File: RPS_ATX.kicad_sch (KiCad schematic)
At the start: 32 parts, among them J1 5V, J2 C1, J3 C2, J4 17.5V, J5 PS_OUT-, J6 PS_OUT+, J7 RPS_OUT+, J9 RPS_OUT-, Q1 AO3400A, U2 AMS1117-3.3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

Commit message: approximate location of the components at the PCB
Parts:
- removed C17: 100n, Capacitor_SMD:C_0805_2012Metric_Pad1.18x1.45mm_HandSolder, symbol Device:C
- added R20: 5.1K, Resistor_SMD:R_1206_3216Metric_Pad1.30x1.75mm_HandSolder, symbol Device:R
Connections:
- net MCU_DCH: now also R20.2
- net MEAS_I+: now also R20.1
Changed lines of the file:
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@@
 	)
 	(junction
+		(at 111.76 63.5)
+		(diameter 0)
+		(color 0 0 0 0)
+	)
+	(junction
 		(at 208.28 30.48)
 		(diameter 0)
@@
 	)
 	(junction
+		(at 111.76 55.88)
+		(diameter 0)
+		(color 0 0 0 0)
+	)
+	(junction
 		(at 63.5 87.63)
 		(diameter 0)
@@
 	)
 	(junction
-		(at 24.13 87.63)
-		(diameter 0)
-		(color 0 0 0 0)
-	)
-	(junction
 		(at 158.75 88.9)
 		(diameter 0)
@@
 	)
 	(junction
-		(at 31.75 87.63)
-		(diameter 0)
-		(color 0 0 0 0)
-	)
-	(junction
 		(at 73.66 149.86)
 		(diameter 0)
@@
 	)
 	(junction
-		(at 31.75 96.52)
+		(at 63.5 149.86)
 		(diameter 0)
 		(color 0 0 0 0)
 	)
 	(junction
-		(at 63.5 149.86)
+		(at 24.13 87.63)
 		(diameter 0)
 		(color 0 0 0 0)
@@
 	(wire
 		(pts
-			(xy 48.26 39.37) (xy 128.27 39.37)
+			(xy 24.13 87.63) (xy 24.13 88.9)
 		)
 		(stroke
@@
 	(wire
 		(pts
-			(xy 196.85 30.48) (xy 208.28 30.48)
+			(xy 48.26 39.37) (xy 128.27 39.37)
 		)
 		(stroke
@@
 	(wire
 		(pts
-			(xy 24.13 87.63) (xy 31.75 87.63)
+			(xy 196.85 30.48) (xy 208.28 30.48)
 		)
 		(stroke
@@
 	(wire
 		(pts
-			(xy 31.75 96.52) (xy 48.26 96.52)
-		)
-		(stroke
-			(width 0)
-			(type default)
-		)
-	)
-	(wire
-		(pts
 			(xy 48.26 127) (xy 48.26 129.54)
 		)
@@
 	(wire
 		(pts
-			(xy 31.75 87.63) (xy 31.75 88.9)
+			(xy 48.26 96.52) (xy 63.5 96.52)
 		)
 		(stroke
@@
 	(wire
 		(pts
-			(xy 48.26 96.52) (xy 63.5 96.52)
+			(xy 48.26 49.53) (xy 48.26 48.26)
 		)
 		(stroke
@@
 	(wire
 		(pts
-			(xy 48.26 49.53) (xy 48.26 48.26)
+			(xy 35.56 49.53) (xy 38.1 49.53)
 		)
 		(stroke
@@
 	(wire
 		(pts
-			(xy 35.56 49.53) (xy 38.1 49.53)
+			(xy 48.26 158.75) (xy 48.26 161.29)
 		)
 		(stroke
@@
 	(wire
 		(pts
-			(xy 48.26 158.75) (xy 48.26 161.29)
+			(xy 142.24 63.5) (xy 142.24 49.53)
 		)
 		(stroke
@@
 	(wire
 		(pts
-			(xy 142.24 63.5) (xy 142.24 49.53)
+			(xy 142.24 49.53) (xy 147.32 49.53)
 		)
 		(stroke
@@
 	(wire
 		(pts
-			(xy 142.24 49.53) (xy 147.32 49.53)
+			(xy 74.93 59.69) (xy 73.66 59.69)
 		)
 		(stroke
@@
 	(wire
 		(pts
-			(xy 74.93 59.69) (xy 73.66 59.69)
+			(xy 40.64 87.63) (xy 24.13 87.63)
 		)
 		(stroke
@@
 	(wire
 		(pts
-			(xy 31.75 87.63) (xy 40.64 87.63)
+			(xy 111.76 63.5) (xy 128.27 63.5)
 		)
 		(stroke
@@
 	(wire
 		(pts
-			(xy 24.13 87.63) (xy 24.13 88.9)
-		)
-		(stroke
-			(width 0)
-			(type default)
-		)
-	)
-	(wire
-		(pts
 			(xy 137.16 104.14) (xy 133.35 104.14)
 		)
@@
 	(wire
 		(pts
-			(xy 95.25 63.5) (xy 128.27 63.5)
+			(xy 95.25 63.5) (xy 111.76 63.5)
 		)
 		(stroke
@@
 	(wire
 		(pts
-			(xy 24.13 96.52) (xy 31.75 96.52)
+			(xy 24.13 96.52) (xy 48.26 96.52)
 		)
 		(stroke
@@
 	)
 	(symbol
+		(lib_id "Device:R")
+		(at 111.76 59.69 180)
+		(unit 1)
+		(exclude_from_sim no)
+		(in_bom yes)
+		(on_board yes)
+		(dnp no)
+		(property "Reference" "R20"
+			(at 107.442 65.024 0)
+			(effects
+				(font
+					(size 1.27 1.27)
+				)
+				(justify right)
+			)
+		)
+		(property "Value" "5.1K"
+			(at 107.442 67.564 0)
+			(effects
+				(font
+					(size 1.27 1.27)
+				)
+				(justify right)
+			)
+		)
+		(property "Footprint" "Resistor_SMD:R_1206_3216Metric_Pad1.30x1.75mm_HandSolder"
+			(at 113.538 59.69 90)
+			(effects
+				(font
+					(size 1.27 1.27)
+				)
+				(hide yes)
+			)
+		)
+		(property "Datasheet" "~"
+			(at 111.76 59.69 0)
+			(effects
+				(font
+					(size 1.27 1.27)
+				)
+				(hide yes)
+			)
+		)
+		(property "Description" "Resistor"
+			(at 111.76 59.69 0)
+			(effects
+				(font
+					(size 1.27 1.27)
+				)
+				(hide yes)
+			)
+		)
+		(pin "1"
+		)
+		(pin "2"
+		)
+		(instances
+			(project "RPS_ATX"
+				(path "/485c2fed-5176-4ba8-b79d-ac7eddb44491"
+					(reference "R20")
+					(unit 1)
+				)
+			)
+		)
+	)
+	(symbol
 		(lib_id "power:GND")
 		(at 149.86 96.52 0)
@@
 					(unit 1)
 				)
-			)
-		)
-	)
-	(symbol
-		(lib_id "Device:C")
-		(at 31.75 92.71 0)
-		(unit 1)
-		(exclude_from_sim no)
-		(in_bom yes)
-		(on_board yes)
-		(dnp no)
-		(property "Reference" "C17"
-			(at 35.56 91.4399 0)
-			(effects
-				(font
-					(size 1.27 1.27)
-				)
-				(justify left)
-			)
-		)
-		(property "Value" "100n"
-			(at 35.56 93.9799 0)
-			(effects
-				(font
-					(size 1.27 1.27)
-				)
-				(justify left)
-			)
-		)
-		(property "Footprint" "Capacitor_SMD:C_0805_2012Metric_Pad1.18x1.45mm_HandSolder"
-			(at 32.7152 96.52 0)
-			(effects
-				(font
-					(size 1.27 1.27)
-				)
-				(hide yes)
-			)
-		)
-		(property "Datasheet" "~"
-			(at 31.75 92.71 0)
-			(effects
-				(font
-					(size 1.27 1.27)
-				)
-				(hide yes)
-			)
-		)
-		(property "Description" "Unpolarized capacitor"
-			(at 31.75 92.71 0)
-			(effects
-				(font
-					(size 1.27 1.27)
-				)
-				(hide yes)
-			)
-		)
-		(pin "2"
-		)
-		(pin "1"
-		)
-		(instances
-			(project "RPS_ATX"
-				(path "/485c2fed-5176-4ba8-b79d-ac7eddb44491"
-					(reference "C17")
-					(unit 1)
-				)

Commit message: final location of the power,analog sections
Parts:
- added L1: L, my lib:Resistor_Shunt_L10_D3.7, symbol Device:L
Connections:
- net GND: now also R20.1
- net MEAS_I+: no longer R20.1
- net VOUT: now also L1.2; no longer J6.1 (Pin_1)
- new net: J6.1 (Pin_1), L1.1
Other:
- moved on the sheet: C8, J5, J6, Q1, R10, R20

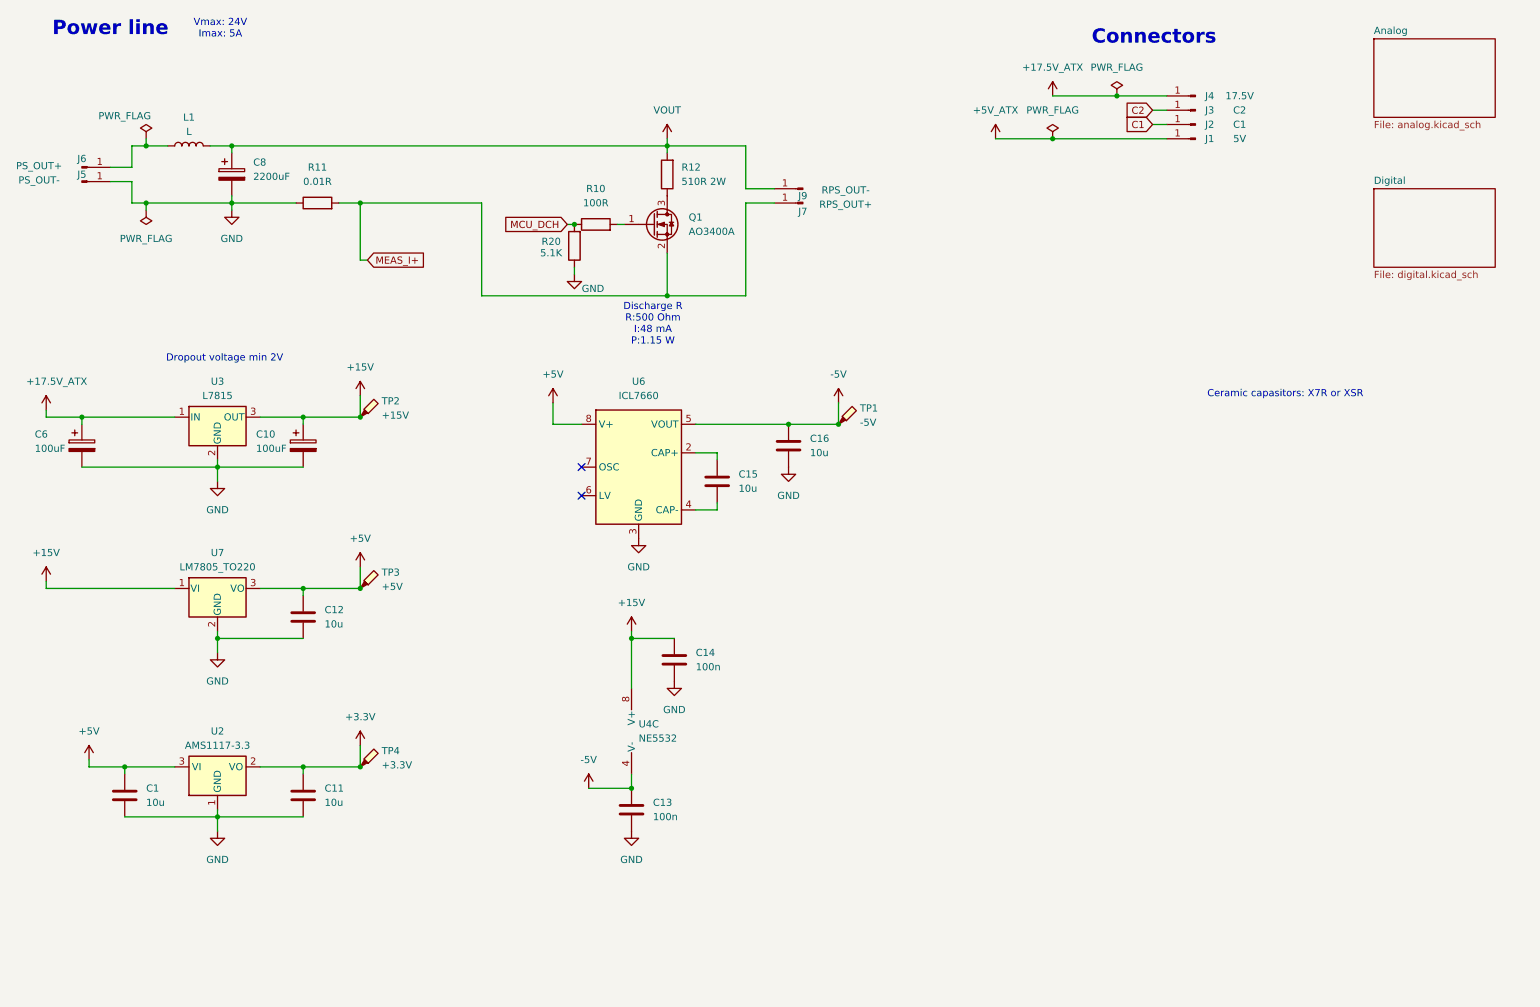
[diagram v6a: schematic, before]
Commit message: added display and encoders signal lines, hints
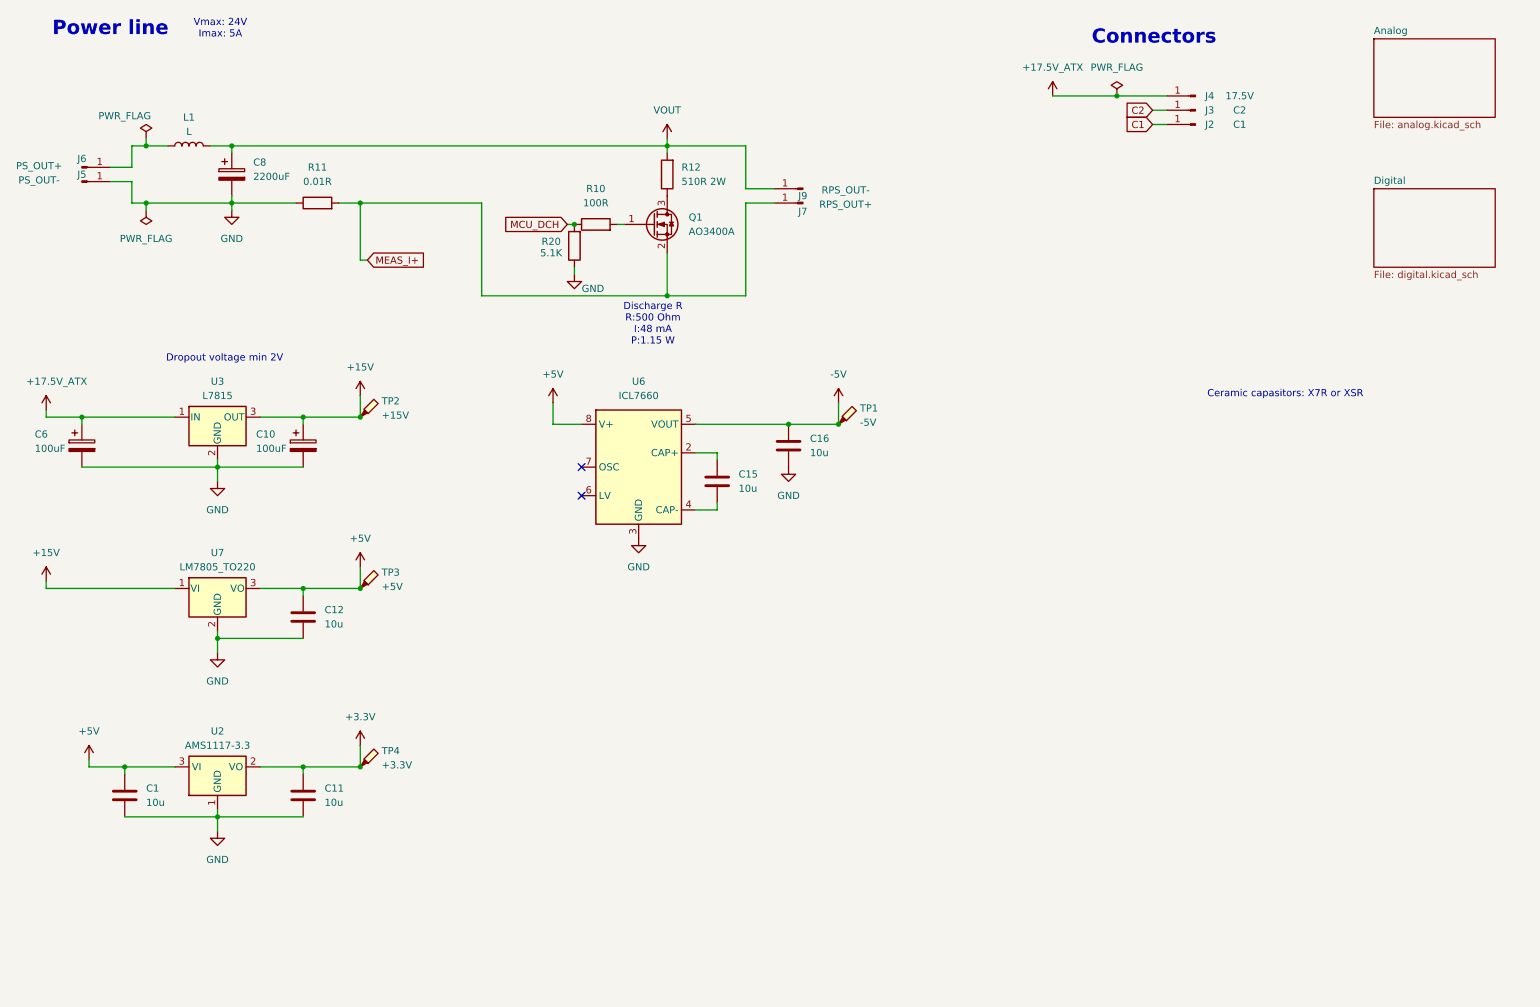
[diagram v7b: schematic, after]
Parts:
- removed C13, C14: 100n, Capacitor_SMD:C_0805_2012Metric_Pad1.18x1.45mm_HandSolder, symbol Device:C
- removed J1: 5V, Connector_PinHeader_2.54mm:PinHeader_1x01_P2.54mm_Vertical, symbol Connector:Conn_01x01_Pin
- removed U4: NE5532, Package_SO:SOIC-8_3.9x4.9mm_P1.27mm, symbol Amplifier_Operational:NE5532

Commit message: added fan control and ds18b20 to the schematic
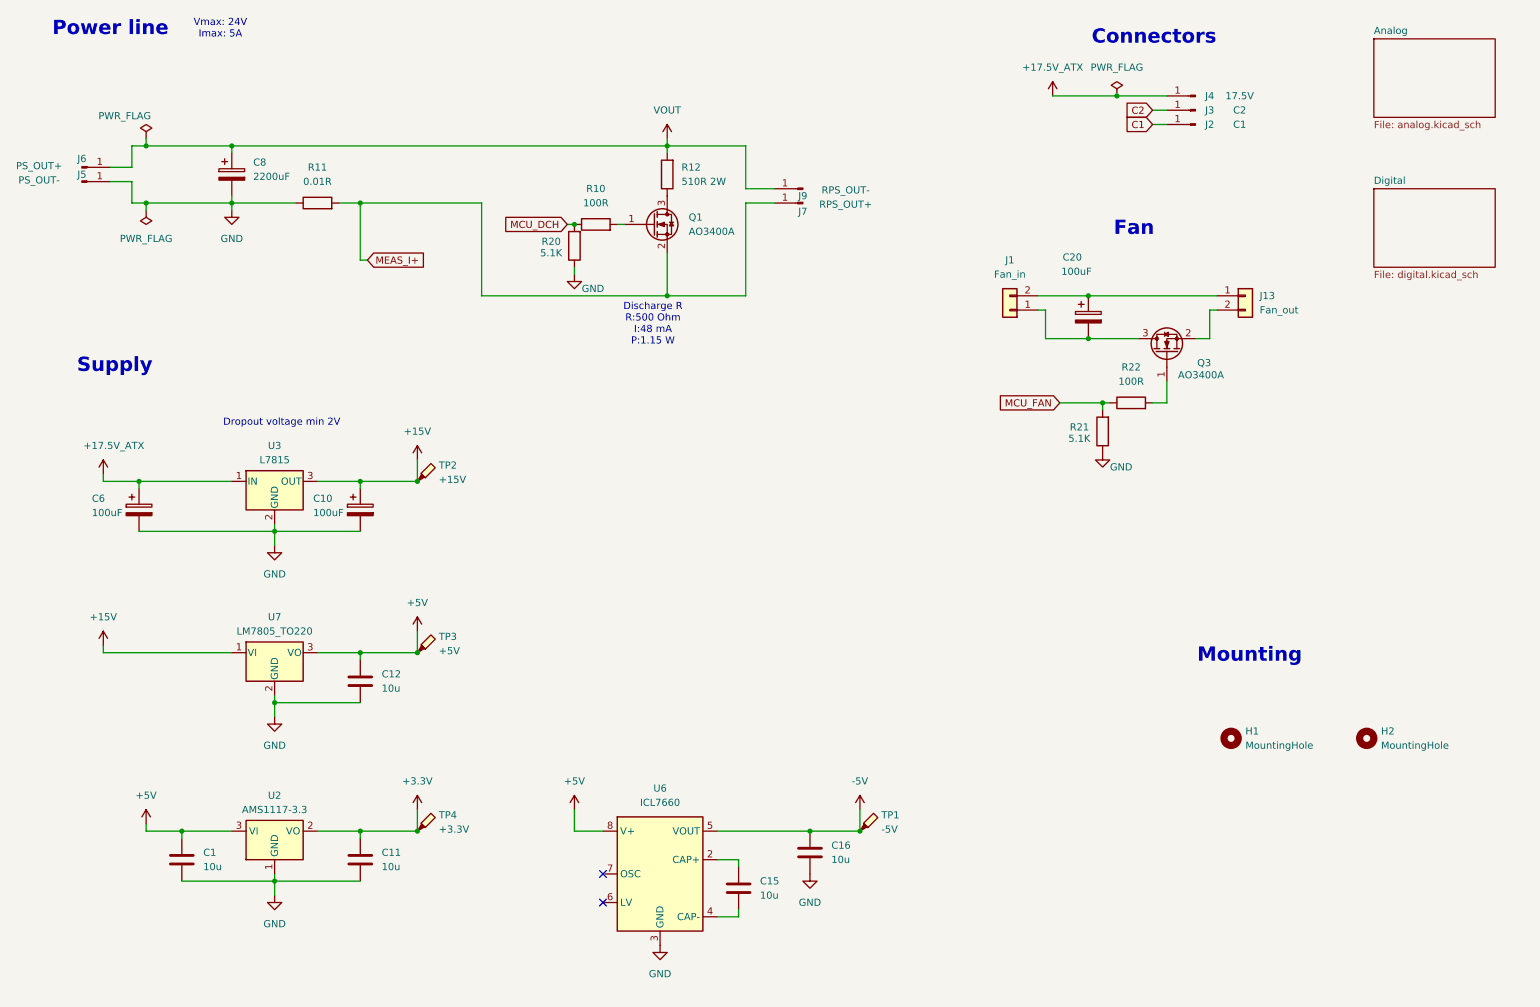
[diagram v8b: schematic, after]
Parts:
- removed L1: L, my lib:Resistor_Shunt_L10_D3.7, symbol Device:L
- added C20: 100uF, Capacitor_SMD:CP_Elec_6.3x5.4_Nichicon, symbol Device:C_Polarized
- added H1, H2: MountingHole, MountingHole:MountingHole_4.3mm_M4, symbol Mechanical:MountingHole
- added J1: Fan_in, Connector_PinHeader_2.54mm:PinHeader_1x02_P2.54mm_Vertical, symbol Connector_Generic:Conn_01x02
- added J13: Fan_out, Connector_PinHeader_2.54mm:PinHeader_1x02_P2.54mm_Vertical, symbol Connector_Generic:Conn_01x02
- added Q3: AO3400A, Package_TO_SOT_SMD:SOT-23, symbol Transistor_FET:AO3400A
- added R21: 5.1K, Resistor_SMD:R_1206_3216Metric_Pad1.30x1.75mm_HandSolder, symbol Device:R
- added R22: 100R, Resistor_SMD:R_1206_3216Metric_Pad1.30x1.75mm_HandSolder, symbol Device:R
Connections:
- net GND: now also R21.1
- net VOUT: now also J6.1 (Pin_1)
- new net: C20.1, J1.2 (Pin_2), J13.1 (Pin_1)
- new net: C20.2, J1.1 (Pin_1), Q3.3 (D)
- new net: J13.2 (Pin_2), Q3.2 (S)
- new net: Q3.1 (G), R22.2
- new net MCU_FAN: R21.2, R22.1
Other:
- note added: "Fan"
- note added: "Mounting"
- note added: "Supply"
- note removed: "Ceramic capasitors: X7R or XSR"
- moved on the sheet: C1, C10, C11, C12, C15, C16, C6, TP1, TP2, TP3, TP4, U2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
